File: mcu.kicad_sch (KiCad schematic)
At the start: 3 parts, among them U2 ESP32-S3-ZERO

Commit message: sd card
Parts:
- added J3: Micro_SD_Card_Module, PEKG:Micro_SD_Card_Module, symbol PEKG_lib:Micro_SD_Card_Module
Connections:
- net GND: now also J3.6 (GND)
- net +3V3: now reaches U2.3V3 (3V3(OUT))
- net +3V3: now also J3.1 (3V3)

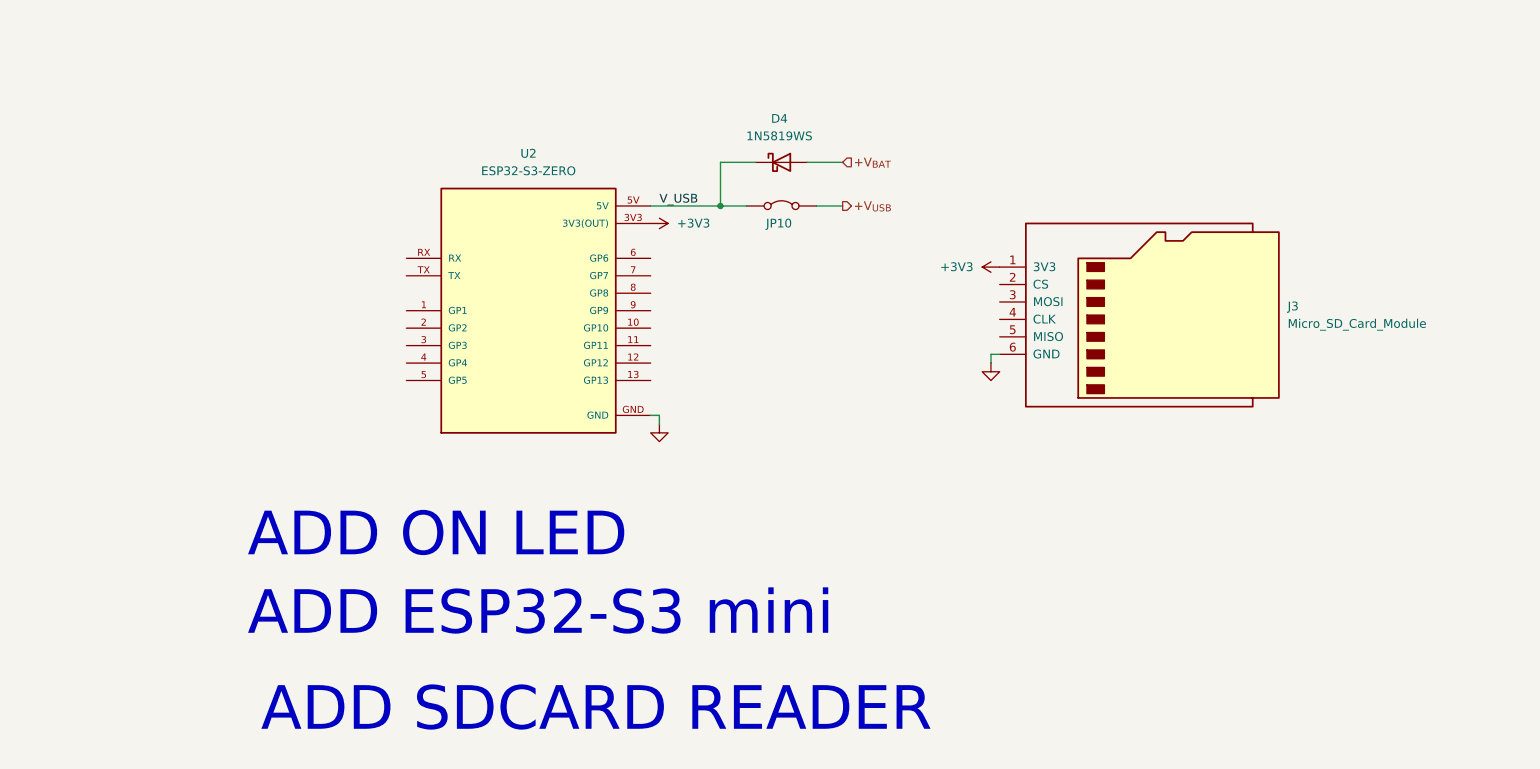
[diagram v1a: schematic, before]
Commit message: connected SD and ESP
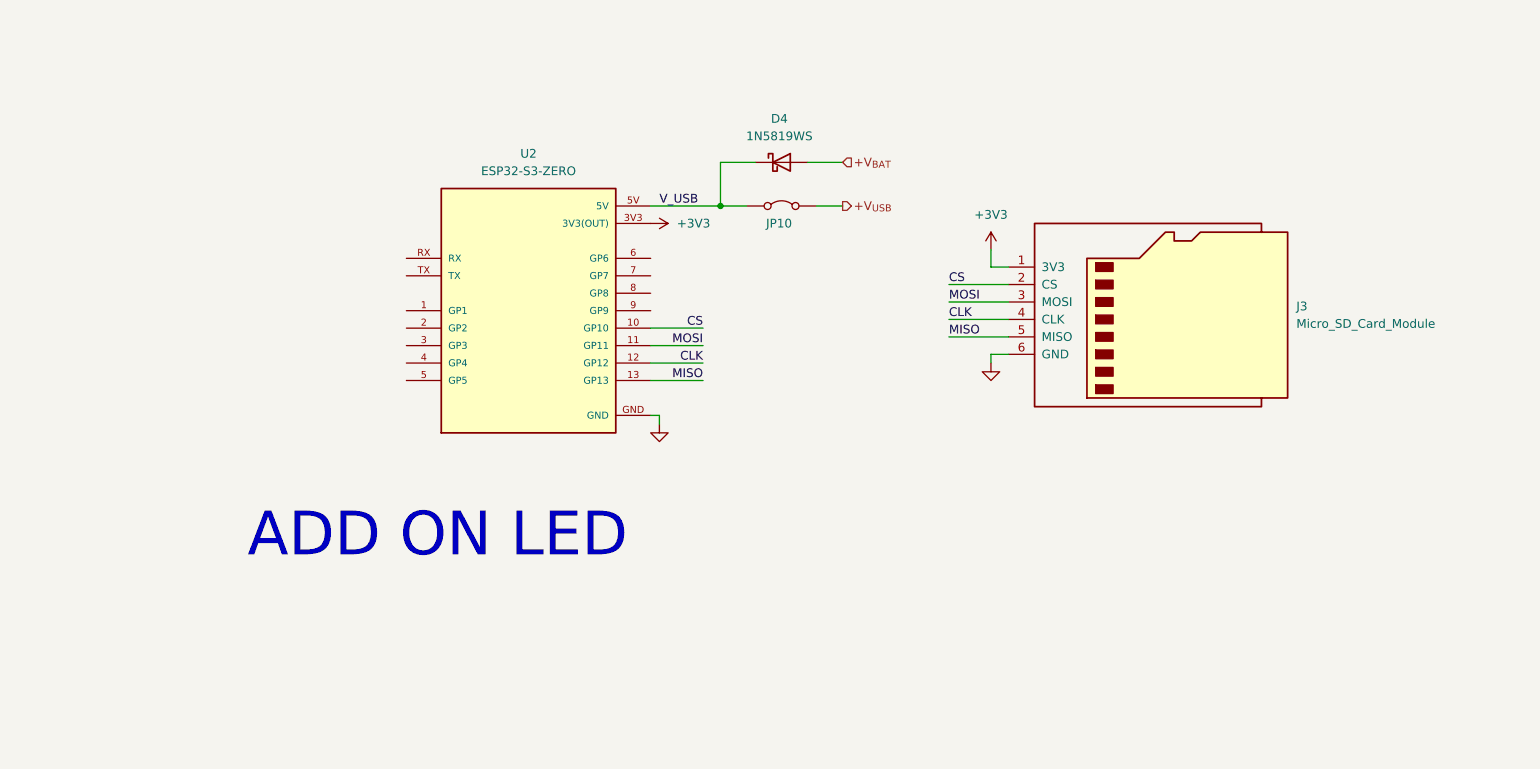
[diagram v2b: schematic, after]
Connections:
- net CS: now reaches J3.2 (CS)
- net CS: now also U2.10 (GP10)
- net MOSI: now reaches J3.3 (MOSI)
- net MOSI: now also U2.11 (GP11)
- net CLK: now reaches J3.4 (CLK)
- net CLK: now also U2.12 (GP12)
- net MISO: now reaches J3.5 (MISO)
- net MISO: now also U2.13 (GP13)
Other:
- note removed: "ADD ESP32-S3 mini"
- note removed: "ADD SDCARD READER"
- moved on the sheet: J3
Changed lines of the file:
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@@
 	(generator_version "9.0")
 	(paper "A4")
-	(text "ADD SDCARD READER\n"
-		(exclude_from_sim no)
-		(at 103.886 133.096 0)
-		(effects
-			(font
-				(size 6.35 6.35)
-			)
-		)
-	)
-	(text "ADD ESP32-S3 mini"
-		(exclude_from_sim no)
-		(at 53.086 119.126 0)
-		(effects
-			(font
-				(size 6.35 6.35)
-			)
-			(justify left)
-		)
-	)
 	(text "ADD ON LED\n"
 		(exclude_from_sim no)
@@
 	(wire
 		(pts
-			(xy 162.56 81.28) (xy 161.29 81.28)
+			(xy 155.1712 71.12) (xy 163.83 71.12)
+		)
+		(stroke
+			(width 0)
+			(type default)
+		)
+	)
+	(wire
+		(pts
+			(xy 161.29 66.04) (xy 161.29 68.58)
+		)
+		(stroke
+			(width 0)
+			(type default)
+		)
+	)
+	(wire
+		(pts
+			(xy 161.29 68.58) (xy 163.83 68.58)
+		)
+		(stroke
+			(width 0)
+			(type default)
+		)
+	)
+	(wire
+		(pts
+			(xy 163.83 81.28) (xy 161.29 81.28)
 		)
 		(stroke
@@
 	(wire
 		(pts
+			(xy 111.76 85.09) (xy 119.38 85.09)
+		)
+		(stroke
+			(width 0)
+			(type default)
+		)
+	)
+	(wire
+		(pts
+			(xy 111.76 80.01) (xy 119.38 80.01)
+		)
+		(stroke
+			(width 0)
+			(type default)
+		)
+	)
+	(wire
+		(pts
 			(xy 121.92 59.69) (xy 125.73 59.69)
 		)
@@
 	(wire
 		(pts
+			(xy 155.1712 73.66) (xy 163.83 73.66)
+		)
+		(stroke
+			(width 0)
+			(type default)
+		)
+	)
+	(wire
+		(pts
 			(xy 121.92 53.34) (xy 121.92 59.69)
 		)
@@
 	(wire
 		(pts
+			(xy 111.76 82.55) (xy 119.38 82.55)
+		)
+		(stroke
+			(width 0)
+			(type default)
+		)
+	)
+	(wire
+		(pts
 			(xy 111.76 59.69) (xy 121.92 59.69)
 		)
@@
 	(wire
 		(pts
+			(xy 155.1712 78.74) (xy 163.83 78.74)
+		)
+		(stroke
+			(width 0)
+			(type default)
+		)
+	)
+	(wire
+		(pts
+			(xy 111.76 77.47) (xy 119.38 77.47)
+		)
+		(stroke
+			(width 0)
+			(type default)
+		)
+	)
+	(wire
+		(pts
 			(xy 134.62 53.34) (xy 139.7 53.34)
 		)
@@
 			(width 0)
 			(type default)
+		)
+	)
+	(wire
+		(pts
+			(xy 155.1712 76.2) (xy 163.83 76.2)
+		)
+		(stroke
+			(width 0)
+			(type default)
+		)
+	)
+	(label "CLK"
+		(at 119.38 82.55 180)
+		(effects
+			(font
+				(size 1.27 1.27)
+			)
+			(justify right bottom)
+		)
+	)
+	(label "MOSI"
+		(at 119.38 80.01 180)
+		(effects
+			(font
+				(size 1.27 1.27)
+			)
+			(justify right bottom)
 		)
 	)
@@
 			)
 			(justify left bottom)
+		)
+	)
+	(label "CS"
+		(at 119.38 77.47 180)
+		(effects
+			(font
+				(size 1.27 1.27)
+			)
+			(justify right bottom)
+		)
+	)
+	(label "MOSI"
+		(at 155.1712 73.66 0)
+		(effects
+			(font
+				(size 1.27 1.27)
+			)
+			(justify left bottom)
+		)
+	)
+	(label "CLK"
+		(at 155.1712 76.2 0)
+		(effects
+			(font
+				(size 1.27 1.27)
+			)
+			(justify left bottom)
+		)
+	)
+	(label "CS"
+		(at 155.1712 71.12 0)
+		(effects
+			(font
+				(size 1.27 1.27)
+			)
+			(justify left bottom)
+		)
+	)
+	(label "MISO"
+		(at 155.1712 78.74 0)
+		(effects
+			(font
+				(size 1.27 1.27)
+			)
+			(justify left bottom)
+		)
+	)
+	(label "MISO"
+		(at 119.38 85.09 180)
+		(effects
+			(font
+				(size 1.27 1.27)
+			)
+			(justify right bottom)
 		)
 	)
@@
 	(symbol
 		(lib_id "PEKG_lib:Micro_SD_Card_Module")
-		(at 182.88 76.2 0)
+		(at 184.15 76.2 0)
 		(unit 1)
 		(exclude_from_sim no)
@@
 		(fields_autoplaced yes)
 		(property "Reference" "J3"
-			(at 204.47 74.2949 0)
+			(at 205.74 74.2949 0)
 			(effects
 				(font
@@
 		)
 		(property "Value" "Micro_SD_Card_Module"
-			(at 204.47 76.8349 0)
+			(at 205.74 76.8349 0)
 			(effects
 				(font
@@
 		)
 		(property "Footprint" "PEKG:Micro_SD_Card_Module"
-			(at 212.09 68.58 0)
+			(at 213.36 68.58 0)
 			(effects
 				(font
@@
 		)
 		(property "Datasheet" "https://www.we-online.com/components/products/datasheet/693072010801.pdf"
-			(at 185.42 76.2 0)
+			(at 186.69 76.2 0)
 			(effects
 				(font
@@
 		)
 		(property "Description" "Micro SD Card Socket"
-			(at 182.88 76.2 0)
+			(at 184.15 76.2 0)
 			(effects
 				(font
@@
 	(symbol
 		(lib_id "power:+3V3")
-		(at 162.56 68.58 90)
+		(at 161.29 66.04 0)
 		(unit 1)
 		(exclude_from_sim no)
@@
 		(fields_autoplaced yes)
 		(property "Reference" "#PWR050"
-			(at 166.37 68.58 0)
+			(at 161.29 69.85 0)
 			(effects
 				(font
@@
 		)
 		(property "Value" "+3V3"
-			(at 158.75 68.5799 90)
-			(effects
-				(font
-					(size 1.27 1.27)
-				)
-				(justify left)
+			(at 161.29 60.96 0)
+			(effects
+				(font
+					(size 1.27 1.27)
+				)
 			)
 		)
 		(property "Footprint" ""
-			(at 162.56 68.58 0)
+			(at 161.29 66.04 0)
 			(effects
 				(font
@@
 		)
 		(property "Datasheet" ""
-			(at 162.56 68.58 0)
+			(at 161.29 66.04 0)
 			(effects
 				(font
@@
 		)
 		(property "Description" "Power symbol creates a global label with name \"+3V3\""
-			(at 162.56 68.58 0)
-			(effects
-				(font
+			(at 161.29 66.04 0)
+			(effects
+				(font

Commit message: updated form factor and placment
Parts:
- added C8: 100n, Capacitor_SMD:C_0603_1608Metric_Pad1.08x0.95mm_HandSolder, symbol Device:C
- added R7: 10k, Resistor_SMD:R_0603_1608Metric_Pad0.98x0.95mm_HandSolder, symbol Device:R
- J3: footprint PEKG:Micro_SD_Card_Module -> PEKG:Micro_SD_Card_Module_UpsideDown_SMD
- U2: footprint PEKG:MODULE_ESP32-S3-ZERO -> PEKG:MODULE_ESP32-S3-ZERO_SMD
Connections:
- net GND: now also C8.1
- net at U2.1 (GP1): now also C8.2, R7.1
- new net ADC1: R7.2

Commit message: ADC, levels
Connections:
- net ADC1 renamed OUTPUT_ADC
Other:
- note added: "ADD ON BLUETOOTH BUTTON, LED ADD PAIR BUTTON, LED"
- note removed: "ADD ON LED"
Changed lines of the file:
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@@
 	(generator_version "9.0")
 	(paper "A4")
-	(text "ADD ON LED\n"
+	(text "ADD ON BLUETOOTH BUTTON, LED\nADD PAIR BUTTON, LED"
 		(exclude_from_sim no)
-		(at 53.086 107.696 0)
+		(at 19.05 120.65 0)
 		(effects
 			(font
@@
 	(wire
 		(pts
+			(xy 163.83 40.64) (xy 163.83 38.1)
+		)
+		(stroke
+			(width 0)
+			(type default)
+		)
+	)
+	(wire
+		(pts
 			(xy 155.1712 73.66) (xy 163.83 73.66)
 		)
@@
 		(pts
 			(xy 60.96 87.63) (xy 60.96 92.71)
+		)
+		(stroke
+			(width 0)
+			(type default)
+		)
+	)
+	(wire
+		(pts
+			(xy 166.37 40.64) (xy 163.83 40.64)
 		)
 		(stroke
@@
 		)
 	)
-	(hierarchical_label "ADC1"
+	(hierarchical_label "+3V3"
+		(shape output)
+		(at 166.37 40.64 0)
+		(effects
+			(font
+				(size 1.27 1.27)
+			)
+			(justify left)
+		)
+	)
+	(hierarchical_label "OUTPUT_ADC"
 		(shape input)
 		(at 44.45 74.93 180)
@@
 					(unit 1)
 				)
+			)
+		)
+	)
+	(symbol
+		(lib_id "power:+3V3")
+		(at 163.83 38.1 0)
+		(unit 1)
+		(exclude_from_sim no)
+		(in_bom yes)
+		(on_board yes)
+		(dnp no)
+		(fields_autoplaced yes)
+		(property "Reference" "#PWR060"
+			(at 163.83 41.91 0)
+			(effects
+				(font
+					(size 1.27 1.27)
+				)
+				(hide yes)
+			)
+		)
+		(property "Value" "+3V3"
+			(at 163.83 33.02 0)
+			(effects
+				(font
+					(size 1.27 1.27)
+				)
+			)
+		)
+		(property "Footprint" ""
+			(at 163.83 38.1 0)
+			(effects
+				(font
+					(size 1.27 1.27)
+				)
+				(hide yes)
+			)
+		)
+		(property "Datasheet" ""
+			(at 163.83 38.1 0)
+			(effects
+				(font
+					(size 1.27 1.27)
+				)
+				(hide yes)
+			)
+		)
+		(property "Description" "Power symbol creates a global label with name \"+3V3\""
+			(at 163.83 38.1 0)
+			(effects
+				(font
+					(size 1.27 1.27)
+				)
+				(hide yes)
+			)
+		)
+		(pin "1"
+		)
+		(instances
+			(project "PEKG"
+				(path "/6b6ace37-3aeb-4177-8f53-de4683f890d9/0d4ea742-5b63-4b37-8bef-d162cee54c1e"
+					(reference "#PWR060")
+					(unit 1)
+				)
